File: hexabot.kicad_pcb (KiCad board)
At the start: 2 copper layers, 100 x 100 mm, 123 parts, among them P1 BATTERY, P10 BUMP2, P11 USB_B, P12 DEBUG, P13 NC, P14 MOTOR_R, P15 MOTOR_L, P16 UART1_5V, P17 ENC1, P18 ENC2, P19 ENC3, P2 EXT_POWER, P20 ENC4, P21 UART2_FTDI3V3, P22 NC, P23 START, P24 DYNAMIXEL2, P25 NC, P26 NC, P27 NC, P3 SERVO1, P4 SERVO2, P5 DYNAMIXEL1, P6 PICKIT, P7 PANIC BUTTON, P8 NC, P9 BUMP1, Q1 Q_NMOS_GSD, Q2 Q_NMOS_GSD, Q3 Q_NMOS_GSD, Q4 Q_NMOS_GSD, SW1 PUSH1, SW2 PUSH2, U1 PTN78020 +5V, U2 PTN78020 SERVO, U3 MCP1727, U4 DSPIC33EP256MU806, U5 L6201PS, U6 L6201PS, Y1 8M

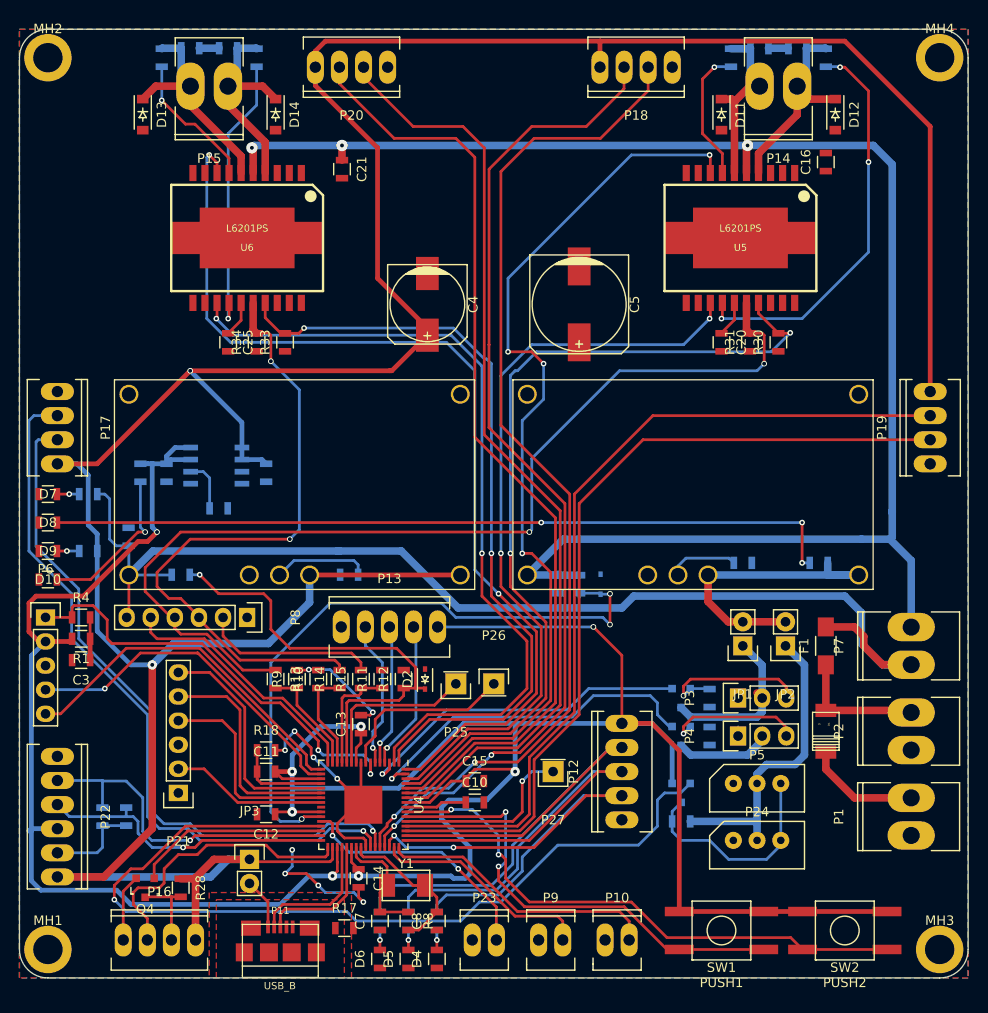
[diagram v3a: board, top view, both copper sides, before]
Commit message: Layout done, check to do, logo to add
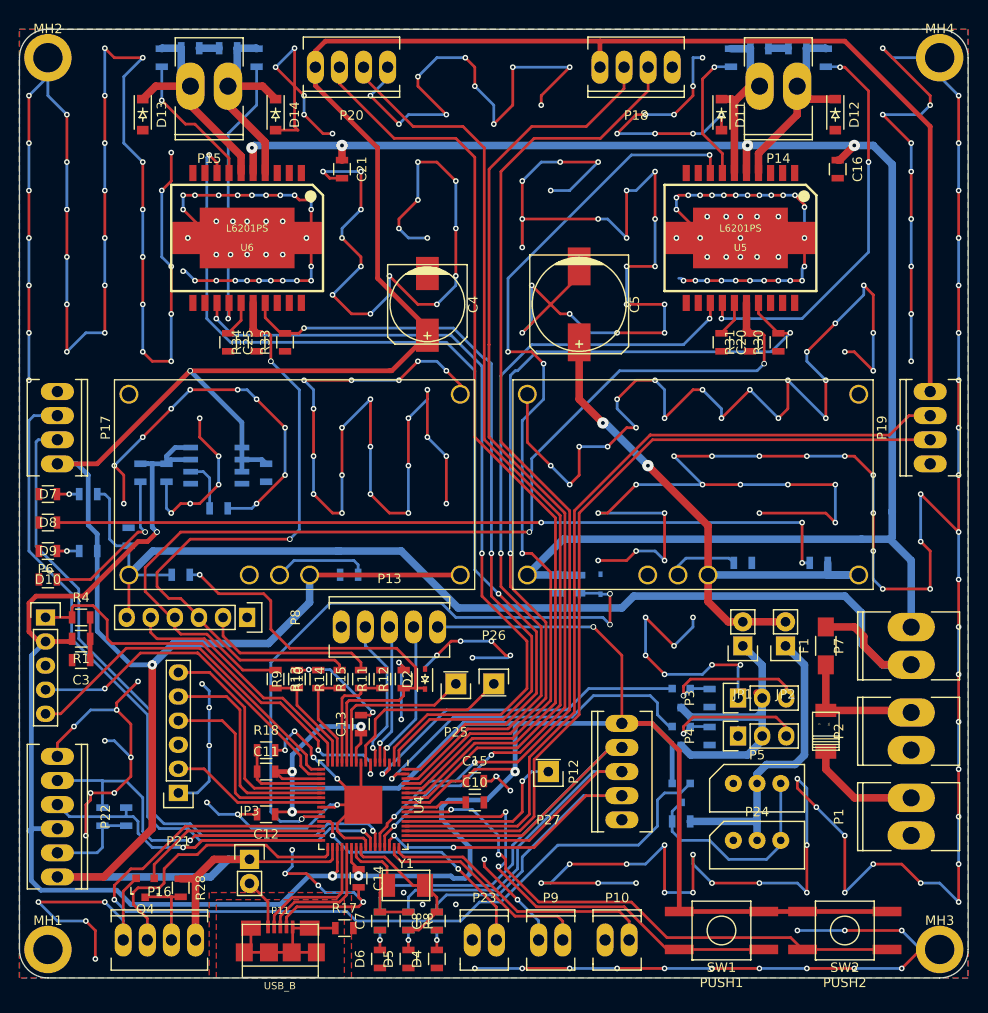
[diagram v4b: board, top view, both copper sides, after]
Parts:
- moved C16 1.46 mm to (186.2, 54.8), turned to 270 degrees
- moved P27 0.50 mm to (155.8, 118.2)
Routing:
- net GND: track 62.8 -> 1491.3 mm, vias 10 -> 343
- net /REG_SERVO: track 32.3 -> 62.6 mm, vias 0 -> 2
- net /USB_SHIELD: track 0.00 -> 17.7 mm
- net (no net): track 0.00 -> 15.1 mm, vias 0 -> 8
- net /PWR_SERVO: track 27.8 -> 31.8 mm
- net /DRIVER_L/MOTOR_POWER: track 171.7 -> 174.1 mm, vias 3 -> 4
- net Net-(P4-Pad3): track 14.4 -> 16.5 mm
- net +5V: track 336.0 -> 337.3 mm
- net /ENC_3_B: track 90.2 -> 89.3 mm
- net /PUSH_1: track 49.4 -> 48.7 mm
- net /PUSH_2: track 59.3 -> 58.7 mm
- net /ENC_3_A: track 88.9 -> 88.3 mm

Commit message: Layout done. Print test to do.
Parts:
- added G***: LOGO, hexabot:hexabot, F.Cu at (150.0, 55.0)
- added LOGO1: OPEN_HARDWARE_1, Symbols:Symbol_OSHW-Logo_SilkScreen, F.Cu at (150.0, 48.0)
- Y1: footprint Crystal_SMD_5x3.2mm -> hexabot:XTAL_5x3.2
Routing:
- net GND: track 1491.3 -> 1531.0 mm, vias 343 -> 352
- net (no net): track 15.1 -> 0.00 mm, vias 8 -> 0
- net /OSC1: track 13.5 -> 11.9 mm
- net /PWR_SERVO: track 31.8 -> 32.5 mm
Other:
- board text added: "3V3"
- board text added: "5V"
- board text added: "Bat"
- board text added: "Controller ver. 0x01 June 2015"
- board text added: "Serv"

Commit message: Few modifs on silk screen gerber generated
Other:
- board text added: "BAT"
- board text added: "Bmp1"
- board text added: "Bmp2"
- board text added: "ENC1"
- board text added: "ENC2"
- board text added: "ENC3"
- board text added: "EXT"
- board text added: "FTDI3V3"
- board text added: "GND"
- board text added: "I2C"
- board text added: "MOTOR_L"
- board text added: "MOTOR_R"
- board text added: "PANIC"
- board text added: "SCL"
- board text added: "SDA"
- board text added: "Start"
- board text added: "UART1"
- board text added: "|3V3"
- board text added: "|5V"

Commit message: Rsense footprintf modified. Anular ring adjusted. Ready to order
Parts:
- R31, R34: footprint Resistors_SMD:R_0805 -> Resistors_SMD:R_1206
- moved R31 0.50 mm to (177.0, 73.5)
- moved R34 0.50 mm to (125.0, 73.5)
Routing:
- net /PWR_SERVO: track 32.5 -> 31.0 mm
- net /DRIVER_R/SENSE: track 106.8 -> 107.7 mm
- net /~PANIC: track 68.1 -> 67.5 mm
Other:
- net class Default: via_drill 0.4 -> 0.3
- rule via_min_drill: 0.3 -> 0.2
